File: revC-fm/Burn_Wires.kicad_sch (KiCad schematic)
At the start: 14 parts, among them K1 PE014006, Q29 MMDT5551-7-F, Q47 MMBT2222LT1G, Q49 BSZ180P03NS3GATMA1, Q50 BSZ180P03NS3GATMA1

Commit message: routing
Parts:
- renumbered Q49 to Q47, Q47 to Q48, R199 to R183, R202 to R184, R196 to R185, R197 to R186, R200 to R187, R201 to R188, R198 to R189
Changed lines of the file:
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@@
   (symbol (lib_id "Device:R_US") (at 158.75 81.28 270) (unit 1)
     (in_bom yes) (on_board yes) (dnp no)
-    (property "Reference" "R198" (at 159.766 85.852 90)
+    (property "Reference" "R189" (at 159.766 85.852 90)
       (effects (font (size 1.27 1.27)) (justify bottom))
     )
@@
       (project "mainboard"
         (path "/d1441985-7b63-4bf8-a06d-c70da2e3b78b/00000000-0000-0000-0000-00005cec6476"
-          (reference "R198") (unit 1)
+          (reference "R189") (unit 1)
         )
       )
@@
   (symbol (lib_id "Device:R_US") (at 45.72 47.625 90) (unit 1)
     (in_bom yes) (on_board yes) (dnp no)
-    (property "Reference" "R196" (at 41.91 43.18 90)
+    (property "Reference" "R185" (at 41.91 43.18 90)
       (effects (font (size 1.27 1.27)) (justify right))
     )
@@
       (project "mainboard"
         (path "/d1441985-7b63-4bf8-a06d-c70da2e3b78b/00000000-0000-0000-0000-00005cec6476"
-          (reference "R196") (unit 1)
+          (reference "R185") (unit 1)
         )
       )
@@
   (symbol (lib_id "Device:R_US") (at 185.42 73.025 90) (unit 1)
     (in_bom yes) (on_board yes) (dnp no)
-    (property "Reference" "R201" (at 194.945 69.85 90)
+    (property "Reference" "R188" (at 194.945 69.85 90)
       (effects (font (size 1.27 1.27)) (justify bottom))
     )
@@
       (project "mainboard"
         (path "/d1441985-7b63-4bf8-a06d-c70da2e3b78b/00000000-0000-0000-0000-00005cec6476"
-          (reference "R201") (unit 1)
+          (reference "R188") (unit 1)
         )
       )
@@
   (symbol (lib_id "SierraLobo:BSZ086") (at 190.5 30.48 270) (mirror x) (unit 1)
     (in_bom yes) (on_board yes) (dnp no)
-    (property "Reference" "Q49" (at 187.96 22.86 90)
+    (property "Reference" "Q47" (at 187.96 22.86 90)
       (effects (font (size 1.27 1.27)) (justify left bottom))
     )
@@
       (project "mainboard"
         (path "/d1441985-7b63-4bf8-a06d-c70da2e3b78b/00000000-0000-0000-0000-00005cec6476"
-          (reference "Q49") (unit 1)
+          (reference "Q47") (unit 1)
         )
       )
@@
   (symbol (lib_id "Device:Q_NPN_BEC") (at 55.88 47.625 0) (unit 1)
     (in_bom yes) (on_board yes) (dnp no)
-    (property "Reference" "Q47" (at 62.23 46.355 0)
+    (property "Reference" "Q48" (at 62.23 46.355 0)
       (effects (font (size 1.27 1.27)) (justify left))
     )
@@
       (project "mainboard"
         (path "/d1441985-7b63-4bf8-a06d-c70da2e3b78b/00000000-0000-0000-0000-00005cec6476"
-          (reference "Q47") (unit 1)
+          (reference "Q48") (unit 1)
         )
       )
@@
   (symbol (lib_id "Device:R_US") (at 186.055 41.91 90) (unit 1)
     (in_bom yes) (on_board yes) (dnp no)
-    (property "Reference" "R202" (at 194.945 42.037 90)
+    (property "Reference" "R184" (at 194.945 42.037 90)
       (effects (font (size 1.27 1.27)) (justify bottom))
     )
@@
       (project "mainboard"
         (path "/d1441985-7b63-4bf8-a06d-c70da2e3b78b/00000000-0000-0000-0000-00005cec6476"
-          (reference "R202") (unit 1)
+          (reference "R184") (unit 1)
         )
       )
@@
   (symbol (lib_id "Device:R_US") (at 158.75 48.26 270) (unit 1)
     (in_bom yes) (on_board yes) (dnp no)
-    (property "Reference" "R197" (at 159.385 52.07 90)
+    (property "Reference" "R186" (at 159.385 52.07 90)
       (effects (font (size 1.27 1.27)) (justify bottom))
     )
@@
       (project "mainboard"
         (path "/d1441985-7b63-4bf8-a06d-c70da2e3b78b/00000000-0000-0000-0000-00005cec6476"
-          (reference "R197") (unit 1)
+          (reference "R186") (unit 1)
         )
       )
@@
   (symbol (lib_id "Device:R_US") (at 170.18 35.56 180) (unit 1)
     (in_bom yes) (on_board yes) (dnp no)
-    (property "Reference" "R199" (at 175.26 32.385 0)
+    (property "Reference" "R183" (at 175.26 32.385 0)
       (effects (font (size 1.27 1.27)) (justify bottom))
     )
@@
       (project "mainboard"
         (path "/d1441985-7b63-4bf8-a06d-c70da2e3b78b/00000000-0000-0000-0000-00005cec6476"
-          (reference "R199") (unit 1)
+          (reference "R183") (unit 1)
         )
       )
@@
   (symbol (lib_id "Device:R_US") (at 170.18 66.04 180) (unit 1)
     (in_bom yes) (on_board yes) (dnp no)
-    (property "Reference" "R200" (at 175.26 63.5 0)
+    (property "Reference" "R187" (at 175.26 63.5 0)
       (effects (font (size 1.27 1.27)) (justify bottom))
     )
@@
       (project "mainboard"
         (path "/d1441985-7b63-4bf8-a06d-c70da2e3b78b/00000000-0000-0000-0000-00005cec6476"
-          (reference "R200") (unit 1)
+          (reference "R187") (unit 1)
         )
       )
@@
   (symbol (lib_id "power:GND") (at 104.14 38.1 0) (unit 1)
     (in_bom yes) (on_board yes) (dnp no)
-    (property "Reference" "#PWR0144" (at 104.14 44.45 0)
+    (property "Reference" "#PWR0138" (at 104.14 44.45 0)
       (effects (font (size 1.27 1.27)) hide)
     )
@@
       (project "mainboard"
         (path "/d1441985-7b63-4bf8-a06d-c70da2e3b78b/00000000-0000-0000-0000-00005cec6476"
-          (reference "#PWR0144") (unit 1)
+          (reference "#PWR0138") (unit 1)
         )
       )
@@
   (symbol (lib_id "power:GND") (at 170.18 53.34 0) (unit 1)
     (in_bom yes) (on_board yes) (dnp no)
-    (property "Reference" "#PWR0145" (at 170.18 59.69 0)
+    (property "Reference" "#PWR0139" (at 170.18 59.69 0)
       (effects (font (size 1.27 1.27)) hide)
     )
@@
       (project "mainboard"
         (path "/d1441985-7b63-4bf8-a06d-c70da2e3b78b/00000000-0000-0000-0000-00005cec6476"
-          (reference "#PWR0145") (unit 1)
+          (reference "#PWR0139") (unit 1)
         )
       )
@@
   (symbol (lib_id "power:GND") (at 58.42 55.88 0) (unit 1)
     (in_bom yes) (on_board yes) (dnp no)
-    (property "Reference" "#PWR0143" (at 58.42 62.23 0)
+    (property "Reference" "#PWR0140" (at 58.42 62.23 0)
       (effects (font (size 1.27 1.27)) hide)
     )
@@
       (project "mainboard"
         (path "/d1441985-7b63-4bf8-a06d-c70da2e3b78b/00000000-0000-0000-0000-00005cec6476"
-          (reference "#PWR0143") (unit 1)
+          (reference "#PWR0140") (unit 1)
         )
       )
@@
   (symbol (lib_id "power:GND") (at 170.18 86.36 0) (unit 1)
     (in_bom yes) (on_board yes) (dnp no)
-    (property "Reference" "#PWR0146" (at 170.18 92.71 0)
+    (property "Reference" "#PWR0141" (at 170.18 92.71 0)
       (effects (font (size 1.27 1.27)) hide)
     )
@@
       (project "mainboard"
         (path "/d1441985-7b63-4bf8-a06d-c70da2e3b78b/00000000-0000-0000-0000-00005cec6476"
-          (reference "#PWR0146") (unit 1)
+          (reference "#PWR0141") (unit 1)
         )
       )
@@
         )
         (path "/d1441985-7b63-4bf8-a06d-c70da2e3b78b/00000000-0000-0000-0000-00005cec6476"
-          (reference "Q48") (unit 2)
+          (reference "Q49") (unit 2)
         )
       )
@@
         )
         (path "/d1441985-7b63-4bf8-a06d-c70da2e3b78b/00000000-0000-0000-0000-00005cec6476"
-          (reference "Q48") (unit 1)
-        )
-      )
+          (reference "Q49") (unit 1)
+        )
+      )

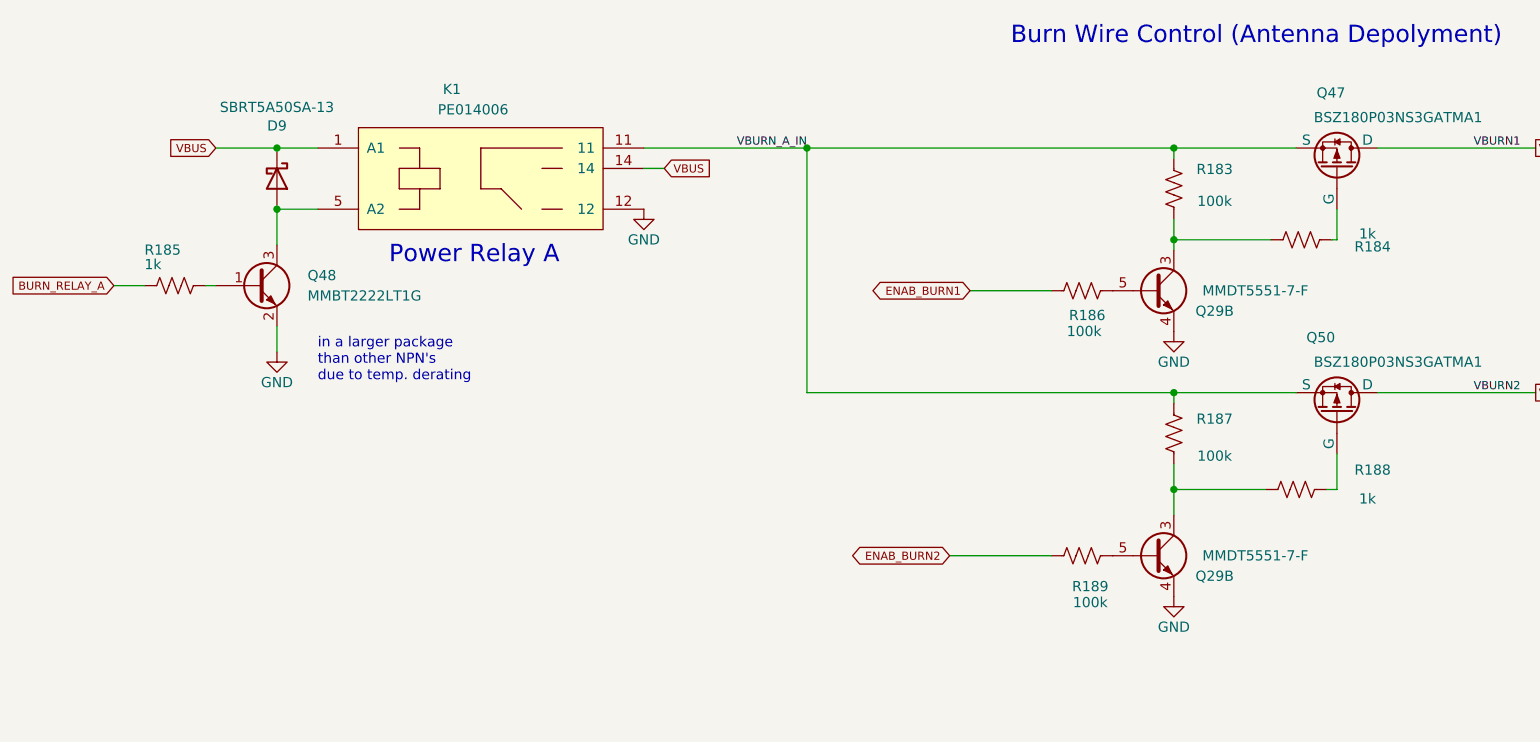
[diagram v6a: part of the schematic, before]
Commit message: changed RF connector to TH
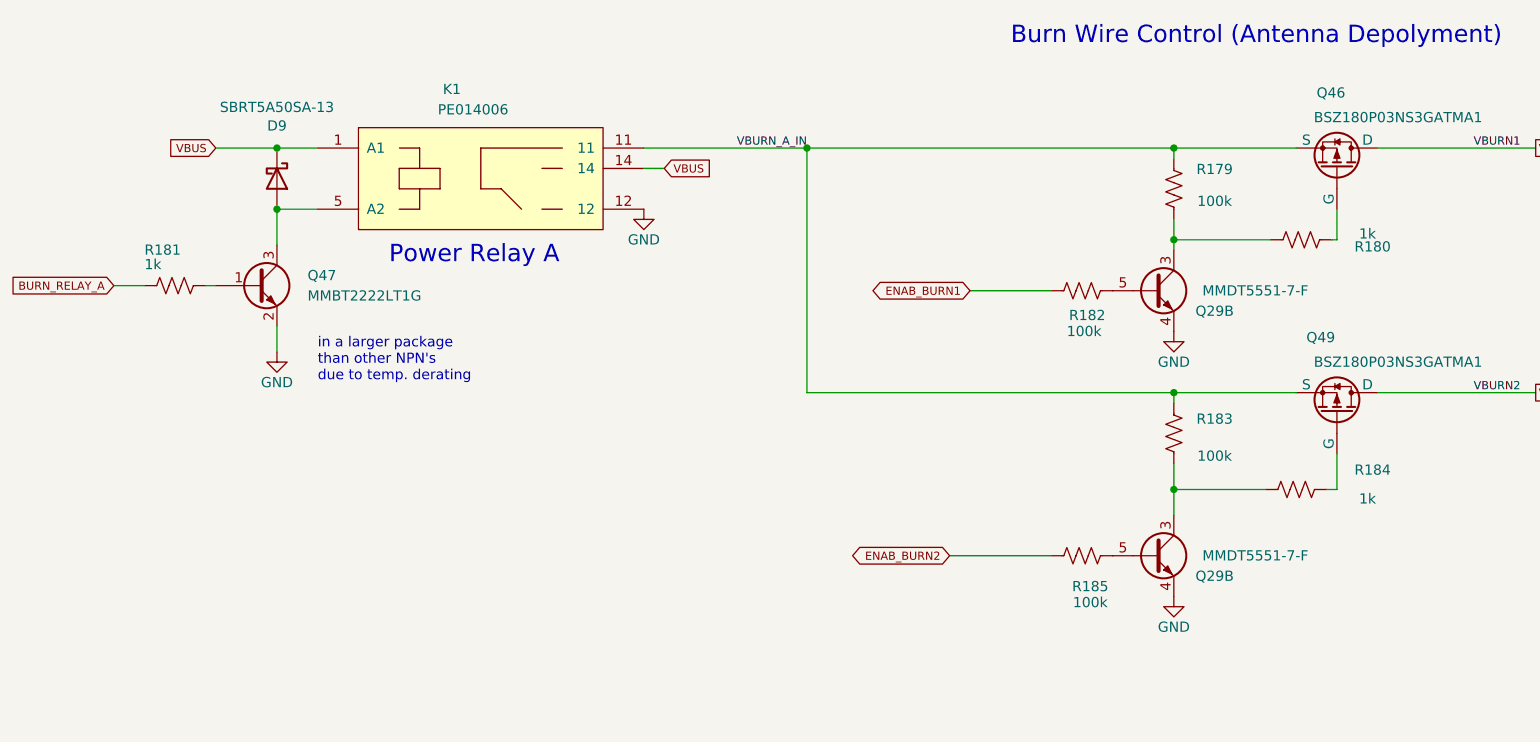
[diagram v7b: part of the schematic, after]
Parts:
- Q47: renamed from Q48; footprint Package_TO_SOT_SMD:SOT-23-3 -> Package_TO_SOT_SMD:SOT-23
- renumbered Q47 to Q46, Q50 to Q49, R183 to R179, R184 to R180, R185 to R181, R186 to R182, R187 to R183, R188 to R184, R189 to R185

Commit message: working revC review changes
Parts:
- renumbered Q46 to Q51, Q47 to Q52, Q49 to Q54, R179 to R194, R180 to R195, R181 to R196, R182 to R197, R183 to R198, R184 to R199, R185 to R200
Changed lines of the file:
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@@
   (symbol (lib_id "Device:R_US") (at 158.75 81.28 270) (unit 1)
     (in_bom yes) (on_board yes) (dnp no)
-    (property "Reference" "R185" (at 159.766 85.852 90)
+    (property "Reference" "R200" (at 159.766 85.852 90)
       (effects (font (size 1.27 1.27)) (justify bottom))
     )
@@
       (project "mainboard"
         (path "/d1441985-7b63-4bf8-a06d-c70da2e3b78b/00000000-0000-0000-0000-00005cec6476"
-          (reference "R185") (unit 1)
+          (reference "R200") (unit 1)
         )
       )
@@
   (symbol (lib_id "Device:R_US") (at 45.72 47.625 90) (unit 1)
     (in_bom yes) (on_board yes) (dnp no)
-    (property "Reference" "R181" (at 41.91 43.18 90)
+    (property "Reference" "R196" (at 41.91 43.18 90)
       (effects (font (size 1.27 1.27)) (justify right))
     )
@@
       (project "mainboard"
         (path "/d1441985-7b63-4bf8-a06d-c70da2e3b78b/00000000-0000-0000-0000-00005cec6476"
-          (reference "R181") (unit 1)
+          (reference "R196") (unit 1)
         )
       )
@@
   (symbol (lib_id "Device:R_US") (at 185.42 73.025 90) (unit 1)
     (in_bom yes) (on_board yes) (dnp no)
-    (property "Reference" "R184" (at 194.945 69.85 90)
+    (property "Reference" "R199" (at 194.945 69.85 90)
       (effects (font (size 1.27 1.27)) (justify bottom))
     )
@@
       (project "mainboard"
         (path "/d1441985-7b63-4bf8-a06d-c70da2e3b78b/00000000-0000-0000-0000-00005cec6476"
-          (reference "R184") (unit 1)
+          (reference "R199") (unit 1)
         )
       )
@@
   (symbol (lib_id "SierraLobo:BSZ086") (at 190.5 30.48 270) (mirror x) (unit 1)
     (in_bom yes) (on_board yes) (dnp no)
-    (property "Reference" "Q46" (at 187.96 22.86 90)
+    (property "Reference" "Q51" (at 187.96 22.86 90)
       (effects (font (size 1.27 1.27)) (justify left bottom))
     )
@@
       (project "mainboard"
         (path "/d1441985-7b63-4bf8-a06d-c70da2e3b78b/00000000-0000-0000-0000-00005cec6476"
-          (reference "Q46") (unit 1)
+          (reference "Q51") (unit 1)
         )
       )
@@
   (symbol (lib_id "SierraLobo:BSZ086") (at 190.5 60.96 270) (mirror x) (unit 1)
     (in_bom yes) (on_board yes) (dnp no)
-    (property "Reference" "Q49" (at 186.69 53.34 90)
+    (property "Reference" "Q54" (at 186.69 53.34 90)
       (effects (font (size 1.27 1.27)) (justify left bottom))
     )
@@
       (project "mainboard"
         (path "/d1441985-7b63-4bf8-a06d-c70da2e3b78b/00000000-0000-0000-0000-00005cec6476"
-          (reference "Q49") (unit 1)
+          (reference "Q54") (unit 1)
         )
       )
@@
   (symbol (lib_id "Device:Q_NPN_BEC") (at 55.88 47.625 0) (unit 1)
     (in_bom yes) (on_board yes) (dnp no)
-    (property "Reference" "Q47" (at 62.23 46.355 0)
+    (property "Reference" "Q52" (at 62.23 46.355 0)
       (effects (font (size 1.27 1.27)) (justify left))
     )
@@
       (project "mainboard"
         (path "/d1441985-7b63-4bf8-a06d-c70da2e3b78b/00000000-0000-0000-0000-00005cec6476"
-          (reference "Q47") (unit 1)
+          (reference "Q52") (unit 1)
         )
       )
@@
   (symbol (lib_id "Device:R_US") (at 186.055 41.91 90) (unit 1)
     (in_bom yes) (on_board yes) (dnp no)
-    (property "Reference" "R180" (at 194.945 42.037 90)
+    (property "Reference" "R195" (at 194.945 42.037 90)
       (effects (font (size 1.27 1.27)) (justify bottom))
     )
@@
       (project "mainboard"
         (path "/d1441985-7b63-4bf8-a06d-c70da2e3b78b/00000000-0000-0000-0000-00005cec6476"
-          (reference "R180") (unit 1)
+          (reference "R195") (unit 1)
         )
       )
@@
   (symbol (lib_id "Device:R_US") (at 158.75 48.26 270) (unit 1)
     (in_bom yes) (on_board yes) (dnp no)
-    (property "Reference" "R182" (at 159.385 52.07 90)
+    (property "Reference" "R197" (at 159.385 52.07 90)
       (effects (font (size 1.27 1.27)) (justify bottom))
     )
@@
       (project "mainboard"
         (path "/d1441985-7b63-4bf8-a06d-c70da2e3b78b/00000000-0000-0000-0000-00005cec6476"
-          (reference "R182") (unit 1)
+          (reference "R197") (unit 1)
         )
       )
@@
   (symbol (lib_id "Device:R_US") (at 170.18 35.56 180) (unit 1)
     (in_bom yes) (on_board yes) (dnp no)
-    (property "Reference" "R179" (at 175.26 32.385 0)
+    (property "Reference" "R194" (at 175.26 32.385 0)
       (effects (font (size 1.27 1.27)) (justify bottom))
     )
@@
       (project "mainboard"
         (path "/d1441985-7b63-4bf8-a06d-c70da2e3b78b/00000000-0000-0000-0000-00005cec6476"
-          (reference "R179") (unit 1)
+          (reference "R194") (unit 1)
         )
       )
@@
   (symbol (lib_id "Device:R_US") (at 170.18 66.04 180) (unit 1)
     (in_bom yes) (on_board yes) (dnp no)
-    (property "Reference" "R183" (at 175.26 63.5 0)
+    (property "Reference" "R198" (at 175.26 63.5 0)
       (effects (font (size 1.27 1.27)) (justify bottom))
     )
@@
       (project "mainboard"
         (path "/d1441985-7b63-4bf8-a06d-c70da2e3b78b/00000000-0000-0000-0000-00005cec6476"
-          (reference "R183") (unit 1)
+          (reference "R198") (unit 1)
         )
       )
@@
   (symbol (lib_id "power:GND") (at 104.14 38.1 0) (unit 1)
     (in_bom yes) (on_board yes) (dnp no)
-    (property "Reference" "#PWR0134" (at 104.14 44.45 0)
+    (property "Reference" "#PWR0140" (at 104.14 44.45 0)
       (effects (font (size 1.27 1.27)) hide)
     )
@@
       (project "mainboard"
         (path "/d1441985-7b63-4bf8-a06d-c70da2e3b78b/00000000-0000-0000-0000-00005cec6476"
-          (reference "#PWR0134") (unit 1)
+          (reference "#PWR0140") (unit 1)
         )
       )
@@
   (symbol (lib_id "power:GND") (at 170.18 53.34 0) (unit 1)
     (in_bom yes) (on_board yes) (dnp no)
-    (property "Reference" "#PWR0135" (at 170.18 59.69 0)
+    (property "Reference" "#PWR0141" (at 170.18 59.69 0)
       (effects (font (size 1.27 1.27)) hide)
     )
@@
       (project "mainboard"
         (path "/d1441985-7b63-4bf8-a06d-c70da2e3b78b/00000000-0000-0000-0000-00005cec6476"
-          (reference "#PWR0135") (unit 1)
+          (reference "#PWR0141") (unit 1)
         )
       )
@@
   (symbol (lib_id "power:GND") (at 58.42 55.88 0) (unit 1)
     (in_bom yes) (on_board yes) (dnp no)
-    (property "Reference" "#PWR0136" (at 58.42 62.23 0)
+    (property "Reference" "#PWR0142" (at 58.42 62.23 0)
       (effects (font (size 1.27 1.27)) hide)
     )
@@
       (project "mainboard"
         (path "/d1441985-7b63-4bf8-a06d-c70da2e3b78b/00000000-0000-0000-0000-00005cec6476"
-          (reference "#PWR0136") (unit 1)
+          (reference "#PWR0142") (unit 1)
         )
       )
@@
   (symbol (lib_id "power:GND") (at 170.18 86.36 0) (unit 1)
     (in_bom yes) (on_board yes) (dnp no)
-    (property "Reference" "#PWR0137" (at 170.18 92.71 0)
+    (property "Reference" "#PWR0143" (at 170.18 92.71 0)
       (effects (font (size 1.27 1.27)) hide)
     )
@@
       (project "mainboard"
         (path "/d1441985-7b63-4bf8-a06d-c70da2e3b78b/00000000-0000-0000-0000-00005cec6476"
-          (reference "#PWR0137") (unit 1)
+          (reference "#PWR0143") (unit 1)
         )
       )
@@
         )
         (path "/d1441985-7b63-4bf8-a06d-c70da2e3b78b/00000000-0000-0000-0000-00005cec6476"
-          (reference "Q48") (unit 2)
+          (reference "Q53") (unit 2)
         )
       )
@@
         )
         (path "/d1441985-7b63-4bf8-a06d-c70da2e3b78b/00000000-0000-0000-0000-00005cec6476"
-          (reference "Q48") (unit 1)
+          (reference "Q53") (unit 1)
         )
       )
@@
         )
         (path "/d1441985-7b63-4bf8-a06d-c70da2e3b78b/00000000-0000-0000-0000-00005cec6476"
-          (reference "D9") (unit 1)
-        )
-      )
+          (reference "D8") (unit 1)
+        )
+      )
